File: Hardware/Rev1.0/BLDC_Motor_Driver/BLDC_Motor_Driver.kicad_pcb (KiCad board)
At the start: 2 copper layers, 2 parts, among them U1 STM32F446RETx, U2 SPB09B-03

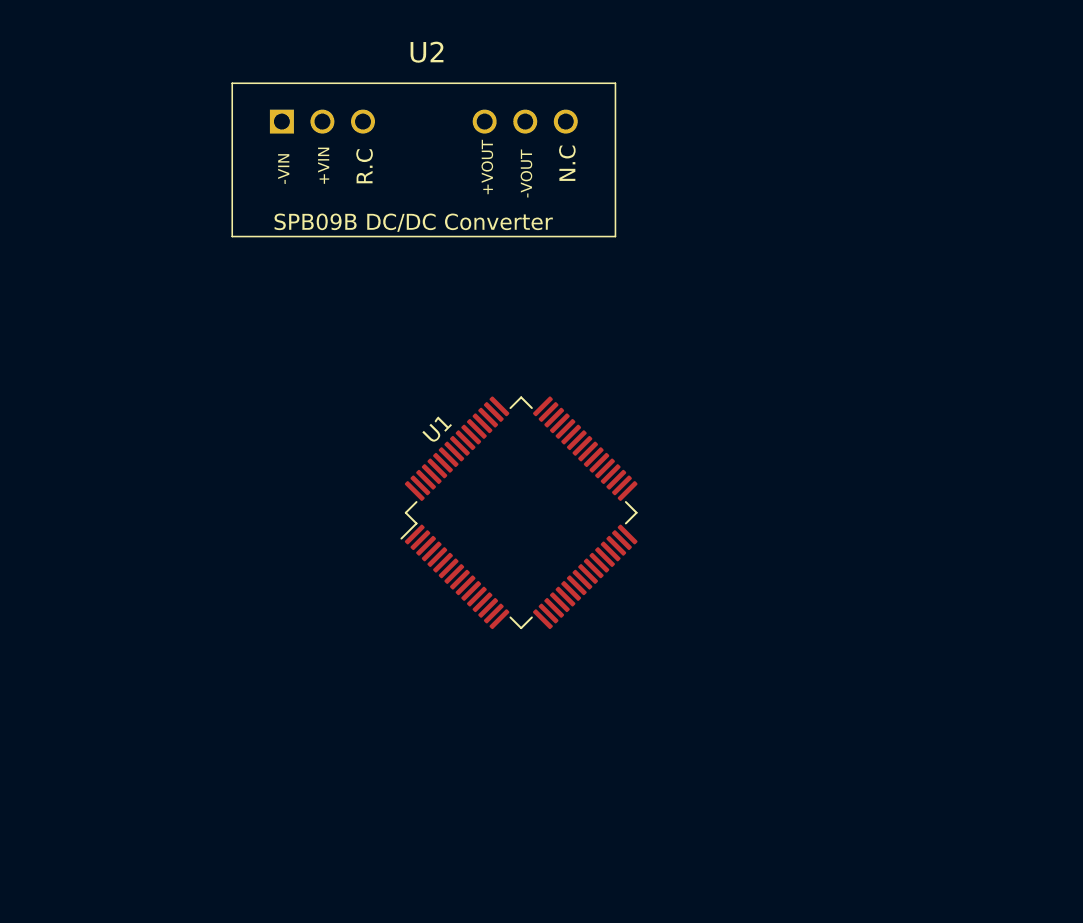
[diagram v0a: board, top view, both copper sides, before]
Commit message: Updates to Stages and MCU inputs
Selected NMOS's and added basis for back EMF
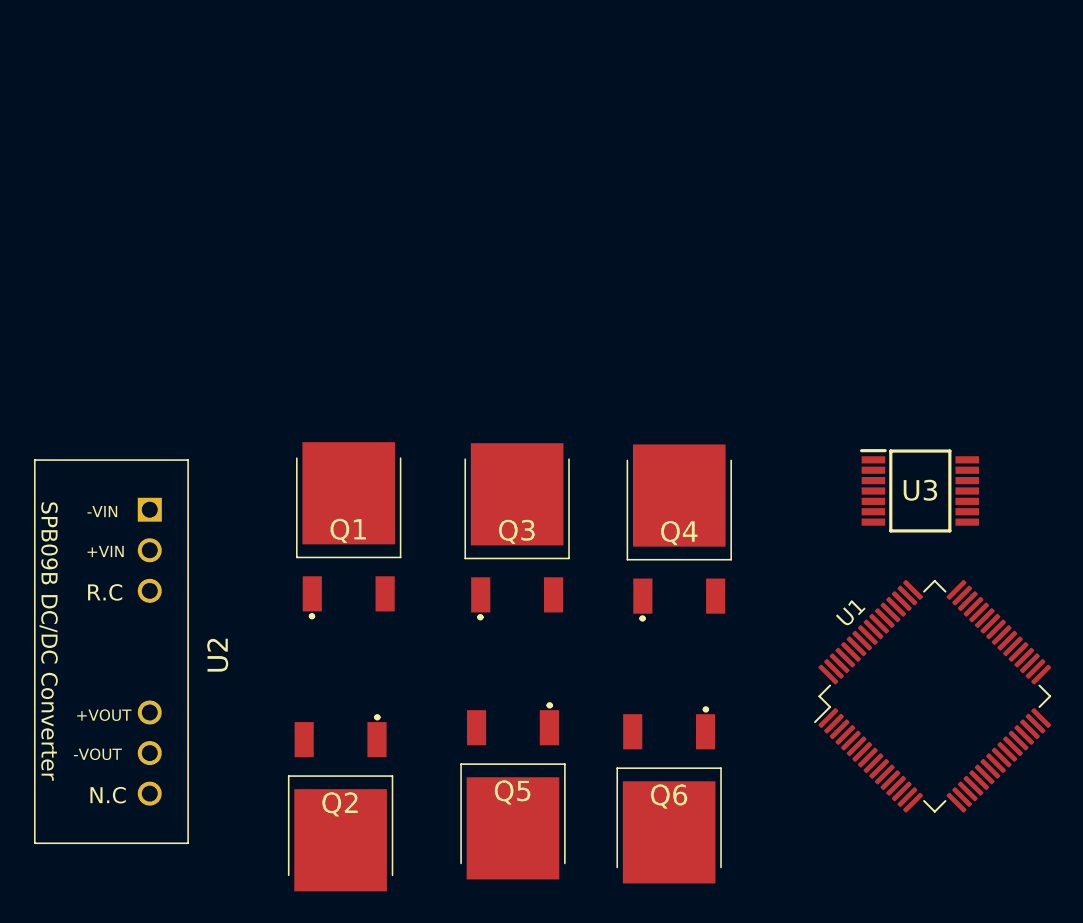
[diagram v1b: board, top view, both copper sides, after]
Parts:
- added Q1: NMOS, Package_TO_SOT_SMD:IPD90N06S4L03, F.Cu at (131.2, 83.6)
- added Q2: NMOS, Package_TO_SOT_SMD:IPD90N06S4L03, F.Cu at (130.7, 99.8)
- added Q3: NMOS, Package_TO_SOT_SMD:IPD90N06S4L03, F.Cu at (141.7, 83.7)
- added Q4: NMOS, Package_TO_SOT_SMD:IPD90N06S4L03, F.Cu at (151.9, 83.8)
- added Q5: NMOS, Package_TO_SOT_SMD:IPD90N06S4L03, F.Cu at (141.5, 99.0)
- added Q6: NMOS, Package_TO_SOT_SMD:IPD90N06S4L03, F.Cu at (151.3, 99.3)
- added U3: TLV1704AQPWRQ1, Package_SO:SOP65P640X120-14N, F.Cu at (167.0, 80.7)
- moved U1 28.3 mm to (167.9, 93.5)
- moved U2 25.7 mm to (118.7, 81.9), turned to -90 degrees

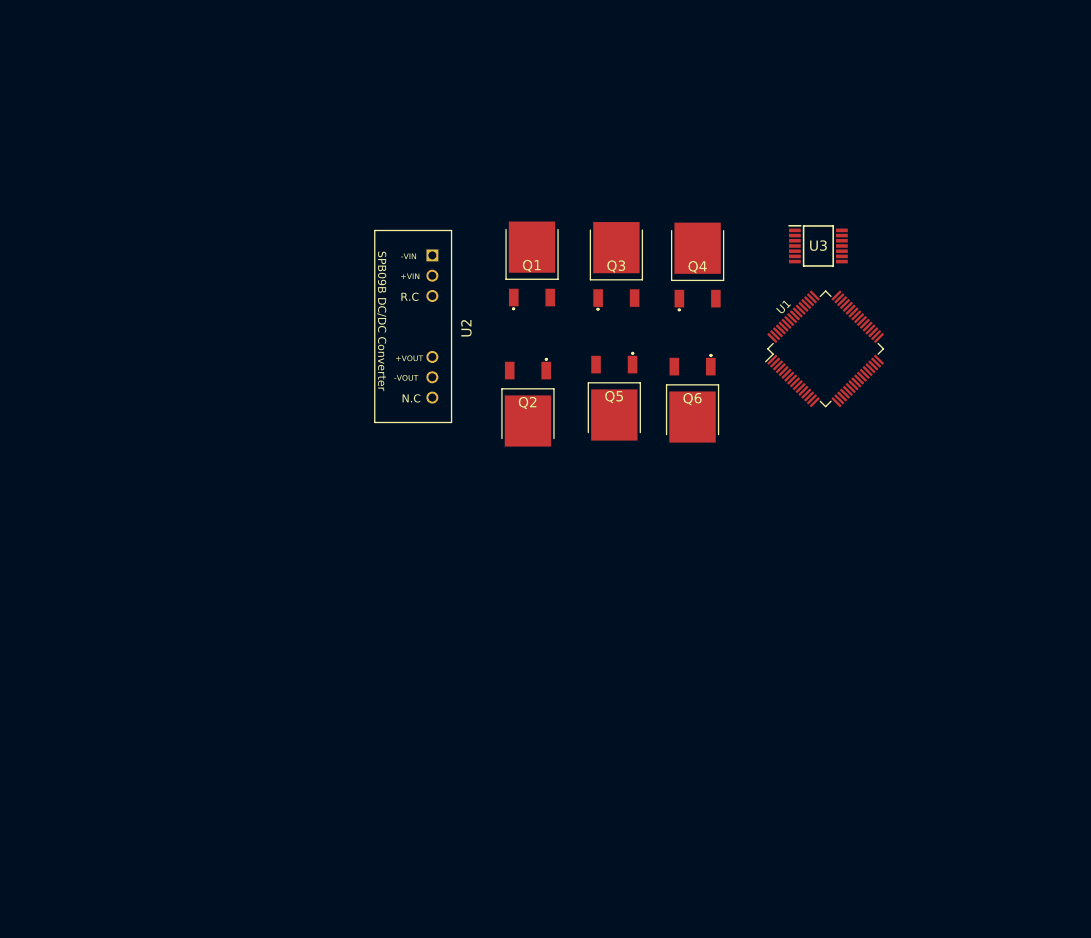
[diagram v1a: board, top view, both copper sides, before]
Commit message: Added changes to schematic (20% competed)
Updated datasheets and schematic symbols for the NMOS FETs. Still need to establish resistor values.
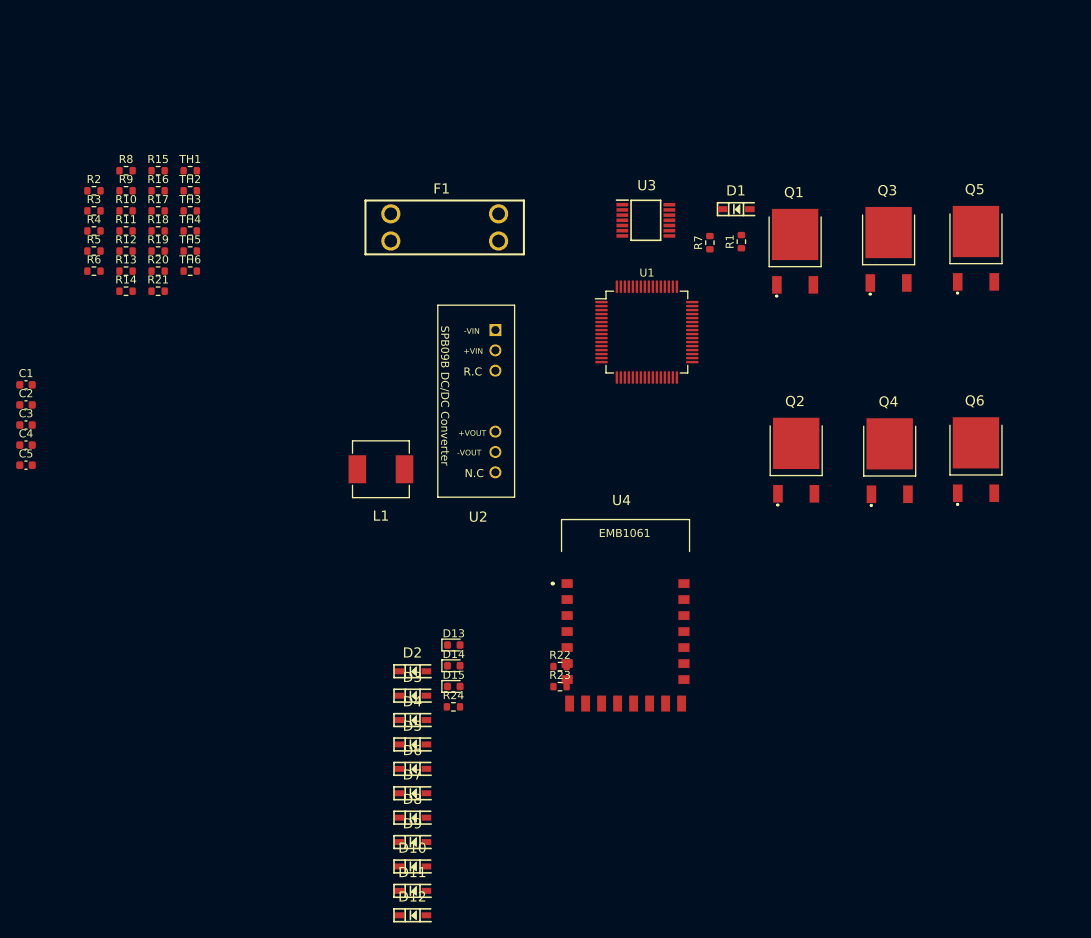
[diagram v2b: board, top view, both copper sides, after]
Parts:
- added C1: 4.7uF, Capacitor_SMD:C_0603_1608Metric, F.Cu at (67.9, 98.0)
- added C2: C_Small, Capacitor_SMD:C_0603_1608Metric, F.Cu at (67.9, 100.5)
- added C3: 2.2uF, Capacitor_SMD:C_0603_1608Metric, F.Cu at (67.9, 103.1)
- added C4: 2.2uF, Capacitor_SMD:C_0603_1608Metric, F.Cu at (67.9, 105.6)
- added C5: 10nF, Capacitor_SMD:C_0603_1608Metric, F.Cu at (67.9, 108.1)
- added D1: 1N5819HWQ-7-F, Diode_SMD:SOD3716X145N, F.Cu at (156.7, 76.1)
- added D10: 1N5819HWQ-7-F, Diode_SMD:SOD3716X145N, F.Cu at (116.3, 158.2)
- added D11: 1N5819HWQ-7-F, Diode_SMD:SOD3716X145N, F.Cu at (116.3, 161.3)
- added D12: 1N5819HWQ-7-F, Diode_SMD:SOD3716X145N, F.Cu at (116.3, 164.3)
- added D13: LED, LED_SMD:LED_0603_1608Metric, F.Cu at (121.4, 130.6)
- added D14: LED, LED_SMD:LED_0603_1608Metric, F.Cu at (121.4, 133.1)
- added D15: LED, LED_SMD:LED_0603_1608Metric, F.Cu at (121.4, 135.7)
- added D2: 1N5819HWQ-7-F, Diode_SMD:SOD3716X145N, F.Cu at (116.3, 133.8)
- added D3: 1N5819HWQ-7-F, Diode_SMD:SOD3716X145N, F.Cu at (116.3, 136.9)
- added D4: 1N5819HWQ-7-F, Diode_SMD:SOD3716X145N, F.Cu at (116.3, 139.9)
- added D5: 1N5819HWQ-7-F, Diode_SMD:SOD3716X145N, F.Cu at (116.3, 143.0)
- added D6: 1N5819HWQ-7-F, Diode_SMD:SOD3716X145N, F.Cu at (116.3, 146.0)
- added D7: 1N5819HWQ-7-F, Diode_SMD:SOD3716X145N, F.Cu at (116.3, 149.1)
- added D8: 1N5819HWQ-7-F, Diode_SMD:SOD3716X145N, F.Cu at (116.3, 152.1)
- added D9: 1N5819HWQ-7-F, Diode_SMD:SOD3716X145N, F.Cu at (116.3, 155.2)
- added F1: BATT_Fuse, Fuse:3557-2, F.Cu at (120.3, 78.4)
- added L1: 10uH, Inductor_SMD:SRP06152R2K, F.Cu at (112.3, 108.6)
- added R1: R_Small, Resistor_SMD:R_0603_1608Metric, F.Cu at (157.4, 80.1)
- added R10: R_Small, Resistor_SMD:R_0603_1608Metric, F.Cu at (80.4, 76.3)
- added R11: R_Small, Resistor_SMD:R_0603_1608Metric, F.Cu at (80.4, 78.8)
- added R12: R_Small, Resistor_SMD:R_0603_1608Metric, F.Cu at (80.4, 81.3)
- added R13: 10kΩ, Resistor_SMD:R_0603_1608Metric, F.Cu at (80.4, 83.8)
- added R14: 10kΩ, Resistor_SMD:R_0603_1608Metric, F.Cu at (80.4, 86.3)
- added R15: 10kΩ, Resistor_SMD:R_0603_1608Metric, F.Cu at (84.4, 71.3)
- added R16: 10kΩ, Resistor_SMD:R_0603_1608Metric, F.Cu at (84.4, 73.8)
- added R17: 10kΩ, Resistor_SMD:R_0603_1608Metric, F.Cu at (84.4, 76.3)
- added R18: 10kΩ, Resistor_SMD:R_0603_1608Metric, F.Cu at (84.4, 78.8)
- added R19: 10kΩ, Resistor_SMD:R_0603_1608Metric, F.Cu at (84.4, 81.3)
- added R2: R_Small, Resistor_SMD:R_0603_1608Metric, F.Cu at (76.4, 73.8)
- added R20: 10kΩ, Resistor_SMD:R_0603_1608Metric, F.Cu at (84.4, 83.8)
- added R21: 10kΩ, Resistor_SMD:R_0603_1608Metric, F.Cu at (84.4, 86.3)
- added R22: 10kΩ, Resistor_SMD:R_0603_1608Metric, F.Cu at (134.7, 133.3)
- added R23: 10kΩ, Resistor_SMD:R_0603_1608Metric, F.Cu at (134.7, 135.8)
- added R24: 10kΩ, Resistor_SMD:R_0603_1608Metric, F.Cu at (121.4, 138.3)
- added R3: R_Small, Resistor_SMD:R_0603_1608Metric, F.Cu at (76.4, 76.3)
- added R4: R_Small, Resistor_SMD:R_0603_1608Metric, F.Cu at (76.4, 78.8)
- added R5: R_Small, Resistor_SMD:R_0603_1608Metric, F.Cu at (76.4, 81.3)
- added R6: R_Small, Resistor_SMD:R_0603_1608Metric, F.Cu at (76.4, 83.8)
- added R7: R_Small, Resistor_SMD:R_0603_1608Metric, F.Cu at (153.4, 80.3)
- added R8: R_Small, Resistor_SMD:R_0603_1608Metric, F.Cu at (80.4, 71.3)
- added R9: R_Small, Resistor_SMD:R_0603_1608Metric, F.Cu at (80.4, 73.8)
- added TH1: PHASE1ATEMP, Resistor_SMD:R_0603_1608Metric, F.Cu at (88.5, 71.3)
- added TH2: PHASE1BTEMP, Resistor_SMD:R_0603_1608Metric, F.Cu at (88.5, 73.8)
- added TH3: PHASE2ATEMP, Resistor_SMD:R_0603_1608Metric, F.Cu at (88.5, 76.3)
- added TH4: PHASE2BTEMP, Resistor_SMD:R_0603_1608Metric, F.Cu at (88.5, 78.8)
- added TH5: PHASE3ATEMP, Resistor_SMD:R_0603_1608Metric, F.Cu at (88.5, 81.3)
- added TH6: PHASE3BTEMP, Resistor_SMD:R_0603_1608Metric, F.Cu at (88.5, 83.8)
- added U4: EMB1061, RF_Module:EMB1061, F.Cu at (142.9, 126.9)
- Q1, Q2, Q3, Q4, Q5, Q6: value NMOS -> IPD90N06S4L03ATMA2
- moved Q5 48.4 mm to (186.7, 81.7), turned to 0 degrees
- moved Q6 36.5 mm to (186.7, 108.1), turned to 0 degrees
- moved Q2 34.6 mm to (164.2, 108.2), turned to 0 degrees
- moved Q4 34.3 mm to (175.9, 108.2)
- moved Q3 34.1 mm to (175.8, 81.8)
- moved Q1 32.9 mm to (164.1, 82.0)
- moved U1 22.4 mm to (145.5, 91.4), turned to 0 degrees
- moved U3 21.8 mm to (145.4, 77.5)
- moved U2 12.2 mm to (126.6, 91.2)

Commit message: Schematic Updates (MOSFETs)
Assigned preliminary rlimit values, modified some footprint placements, and fixed a MOSFET misassignment for schematics.
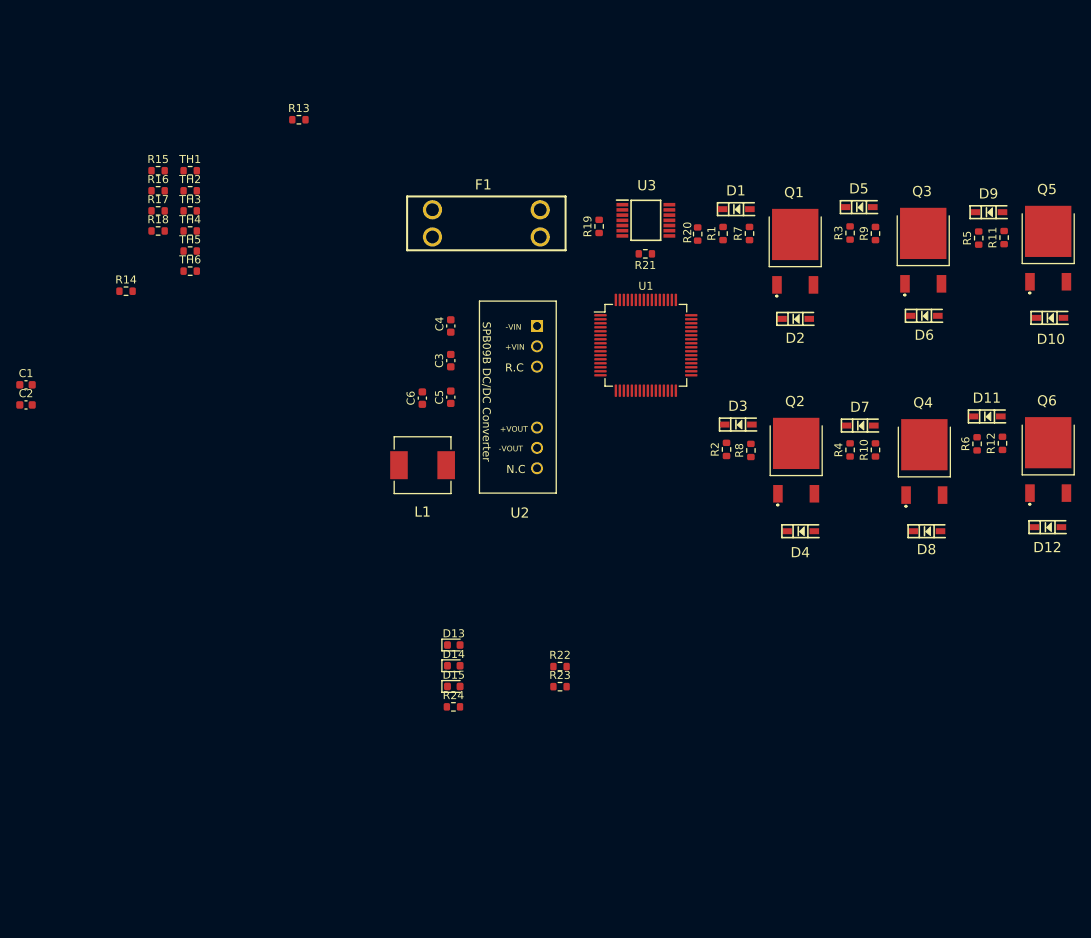
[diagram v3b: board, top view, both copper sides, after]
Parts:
- removed U4: EMB1061, RF_Module:EMB1061
- added C6: 10uF, Capacitor_SMD:C_0603_1608Metric, F.Cu at (117.5, 99.7)
- R1, R10, R11, R12, R2, R3, R4, R5, R6, R7, R8, R9: value R_Small -> 100Ω
- moved R6 112.5 mm to (186.8, 105.4), turned to 90 degrees
- moved R12 112.2 mm to (190.0, 105.3), turned to 90 degrees
- moved R5 110.6 mm to (187.0, 79.7), turned to 90 degrees
- moved R11 109.8 mm to (190.2, 79.6), turned to 90 degrees
- moved D9 106.7 mm to (188.3, 76.5)
- moved D10 105.1 mm to (195.9, 89.7)
- moved R4 98.4 mm to (170.9, 106.2), turned to 90 degrees
- moved R10 98.3 mm to (174.1, 106.2), turned to 90 degrees
- moved R3 94.6 mm to (170.9, 79.1), turned to 90 degrees
- moved R9 93.8 mm to (174.1, 79.1), turned to 90 degrees
- moved D11 93.1 mm to (188.1, 102.0)
- moved D12 93.0 mm to (195.7, 115.8)
- moved D5 87.3 mm to (172.1, 75.8)
- moved R8 85.6 mm to (158.5, 106.2), turned to 90 degrees
- moved R2 85.4 mm to (155.5, 106.1), turned to 90 degrees
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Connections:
- Q1 pad 1: +BATT -> Net-(Q1-Pad1)
- Q1 pad 2: Net-(Q1-Pad2) -> +BATT
- Q2 pad 1: Phase1 -> Net-(Q2-Pad1)
- Q2 pad 2: Net-(Q2-Pad2) -> Phase1
- Q3 pad 1: +BATT -> Net-(Q3-Pad1)
- Q3 pad 2: Net-(Q3-Pad2) -> +BATT
- Q4 pad 1: Phase2 -> Net-(Q4-Pad1)
- Q4 pad 2: Net-(Q4-Pad2) -> Phase2
- Q5 pad 1: +BATT -> Net-(Q5-Pad1)
- Q5 pad 2: Net-(Q5-Pad2) -> +BATT
- Q6 pad 1: Phase3 -> Net-(Q6-Pad1)
- Q6 pad 2: Net-(Q6-Pad2) -> Phase3
- R1 pad 2: Net-(Q1-Pad2) -> Net-(Q1-Pad1)
- R10 pad 2: Net-(Q4-Pad2) -> Net-(Q4-Pad1)
- R11 pad 2: Net-(Q5-Pad2) -> Net-(Q5-Pad1)
- R12 pad 2: Net-(Q6-Pad2) -> Net-(Q6-Pad1)
- R2 pad 2: Net-(Q2-Pad2) -> Net-(Q2-Pad1)
- R3 pad 2: Net-(Q3-Pad2) -> Net-(Q3-Pad1)
- R4 pad 2: Net-(Q4-Pad2) -> Net-(Q4-Pad1)
- R5 pad 2: Net-(Q5-Pad2) -> Net-(Q5-Pad1)
- R6 pad 2: Net-(Q6-Pad2) -> Net-(Q6-Pad1)
- R7 pad 2: Net-(Q1-Pad2) -> Net-(Q1-Pad1)
- R8 pad 2: Net-(Q2-Pad2) -> Net-(Q2-Pad1)
- R9 pad 2: Net-(Q3-Pad2) -> Net-(Q3-Pad1)
